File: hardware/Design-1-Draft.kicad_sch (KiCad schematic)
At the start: 32 parts, among them J1 Barrel_Jack_Switch, M1 WATERPUMP-2, M2 WATERPUMP-1, Q1 IRLZ44N, Q2 IRLZ44N, SW1 Button, U1 ADS1115IDGS, U2 Tang_Nano_9K

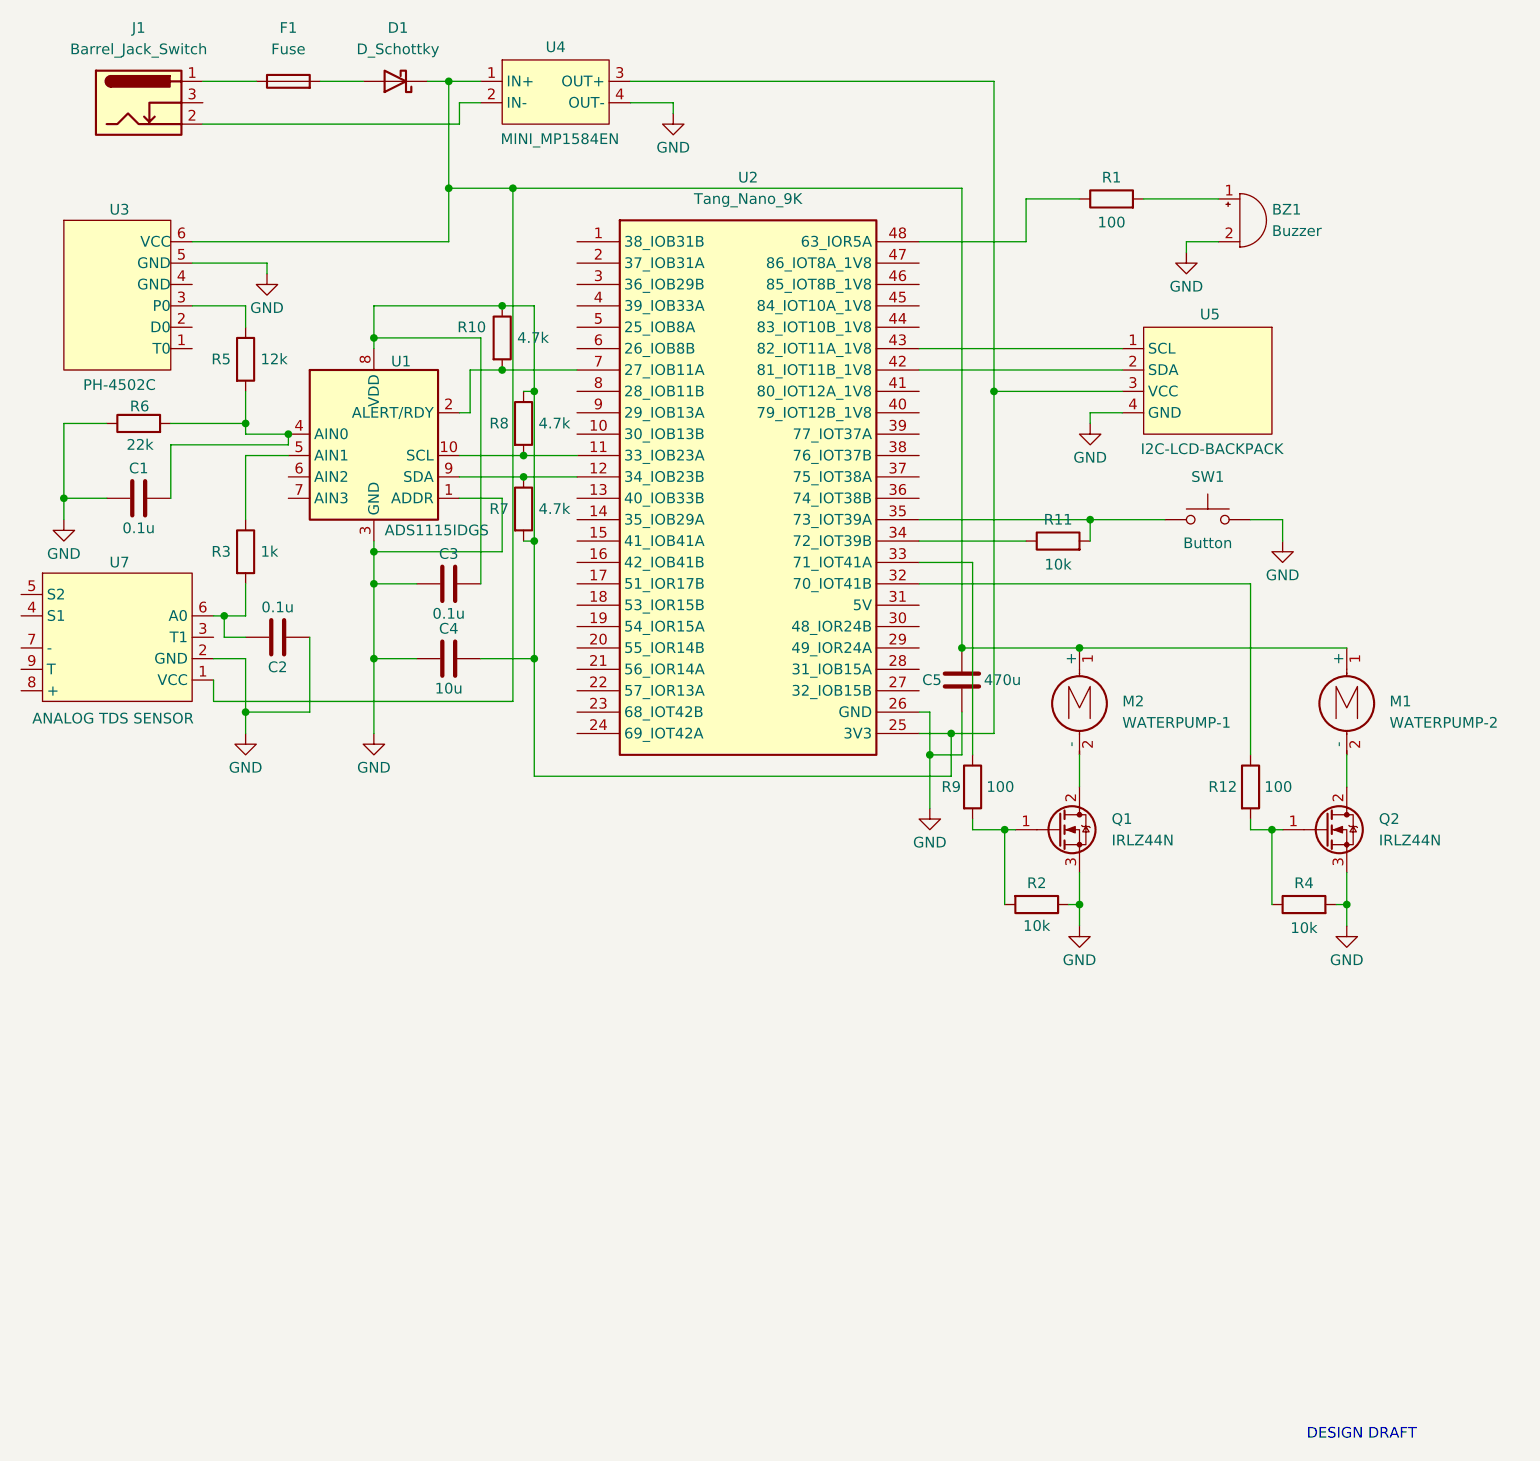
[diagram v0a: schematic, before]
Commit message: Renaming Symbols
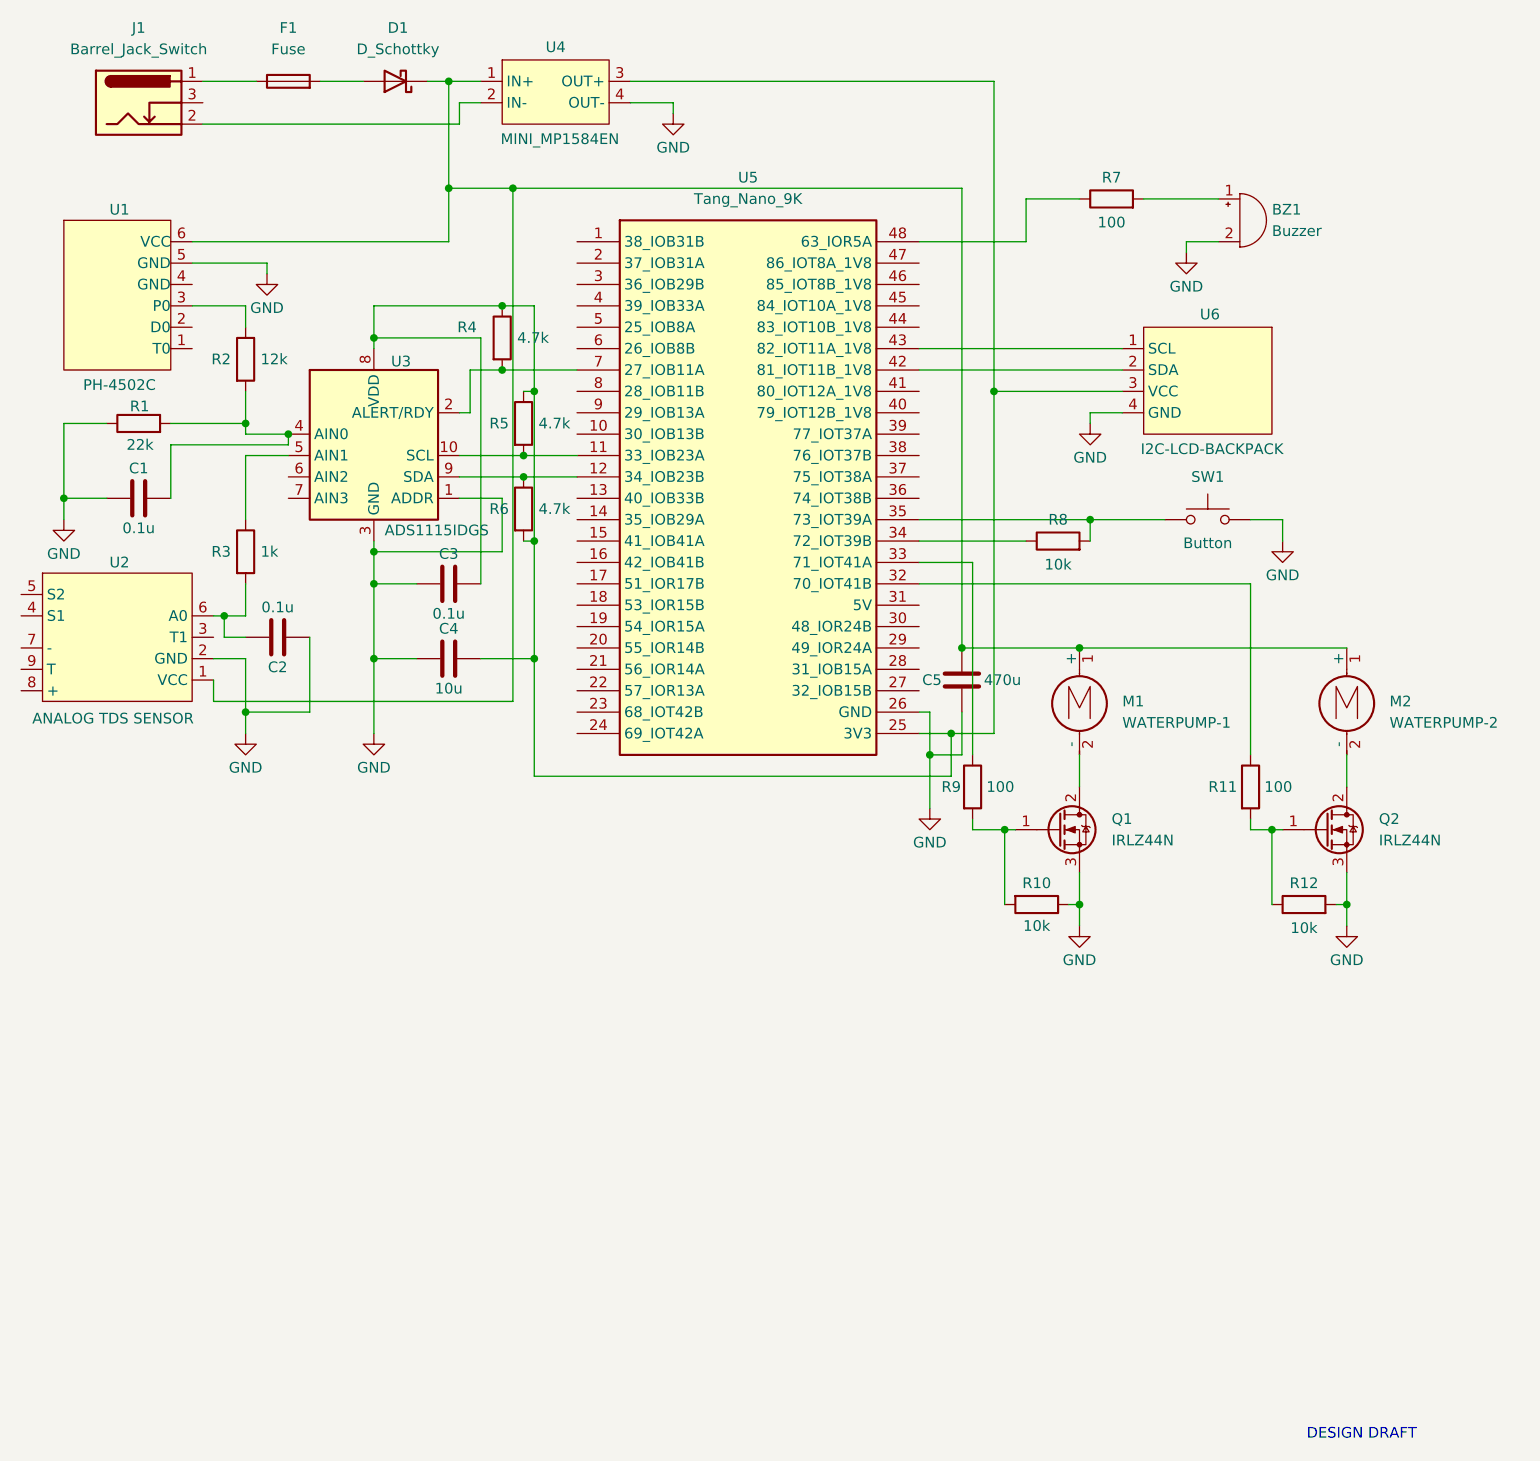
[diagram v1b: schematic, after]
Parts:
- renumbered M2 to M1, M1 to M2, R6 to R1, R2 to R10, R12 to R11, R4 to R12, R5 to R2, R10 to R4, R8 to R5, R7 to R6, R1 to R7, R11 to R8, U3 to U1, U7 to U2, U1 to U3, U2 to U5, U5 to U6
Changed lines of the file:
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@@
 		(on_board yes)
 		(dnp no)
-		(property "Reference" "R2"
+		(property "Reference" "R10"
 			(at 154.94 124.46 90)
 			(effects
@@
 			(project "Design-1-Draft"
 				(path "/9fcc7f51-9e94-44d9-a052-14e93dbf110b"
-					(reference "R2")
+					(reference "R10")
 					(unit 1)
 				)
@@
 		(on_board yes)
 		(dnp no)
-		(property "Reference" "U7"
+		(property "Reference" "U2"
 			(at 45.974 86.36 0)
 			(effects
@@
 			(project ""
 				(path "/9fcc7f51-9e94-44d9-a052-14e93dbf110b"
-					(reference "U7")
+					(reference "U2")
 					(unit 1)
 				)
@@
 		(on_board yes)
 		(dnp no)
-		(property "Reference" "R1"
+		(property "Reference" "R7"
 			(at 163.83 40.64 90)
 			(effects
@@
 			(project "Design-1-Draft"
 				(path "/9fcc7f51-9e94-44d9-a052-14e93dbf110b"
-					(reference "R1")
+					(reference "R7")
 					(unit 1)
 				)
@@
 		(on_board yes)
 		(dnp no)
-		(property "Reference" "R6"
+		(property "Reference" "R1"
 			(at 49.53 67.818 90)
 			(effects
@@
 			(project "Design-1-Draft"
 				(path "/9fcc7f51-9e94-44d9-a052-14e93dbf110b"
-					(reference "R6")
+					(reference "R1")
 					(unit 1)
 				)
@@
 		(on_board yes)
 		(dnp no)
-		(property "Reference" "R8"
+		(property "Reference" "R5"
 			(at 89.916 69.85 0)
 			(effects
@@
 			(project "Design-1-Draft"
 				(path "/9fcc7f51-9e94-44d9-a052-14e93dbf110b"
-					(reference "R8")
+					(reference "R5")
 					(unit 1)
 				)
@@
 		(on_board yes)
 		(dnp no)
-		(property "Reference" "R10"
+		(property "Reference" "R4"
 			(at 86.106 58.42 0)
 			(effects
@@
 			(project "Design-1-Draft"
 				(path "/9fcc7f51-9e94-44d9-a052-14e93dbf110b"
-					(reference "R10")
+					(reference "R4")
 					(unit 1)
 				)
@@
 		(dnp no)
 		(fields_autoplaced yes)
-		(property "Reference" "U2"
+		(property "Reference" "U5"
 			(at 120.65 40.64 0)
 			(effects
@@
 			(project ""
 				(path "/9fcc7f51-9e94-44d9-a052-14e93dbf110b"
-					(reference "U2")
+					(reference "U5")
 					(unit 1)
 				)
@@
 		(dnp no)
 		(fields_autoplaced yes)
-		(property "Reference" "M1"
+		(property "Reference" "M2"
 			(at 196.85 102.8699 0)
 			(effects
@@
 			(project ""
 				(path "/9fcc7f51-9e94-44d9-a052-14e93dbf110b"
-					(reference "M1")
+					(reference "M2")
 					(unit 1)
 				)
@@
 		(on_board yes)
 		(dnp no)
-		(property "Reference" "R7"
+		(property "Reference" "R6"
 			(at 89.916 80.01 0)
 			(effects
@@
 			(project "Design-1-Draft"
 				(path "/9fcc7f51-9e94-44d9-a052-14e93dbf110b"
-					(reference "R7")
+					(reference "R6")
 					(unit 1)
 				)
@@
 		(dnp no)
 		(fields_autoplaced yes)
-		(property "Reference" "M2"
+		(property "Reference" "M1"
 			(at 165.1 102.8699 0)
 			(effects
@@
 			(project ""
 				(path "/9fcc7f51-9e94-44d9-a052-14e93dbf110b"
-					(reference "M2")
+					(reference "M1")
 					(unit 1)
 				)
@@
 		(on_board yes)
 		(dnp no)
-		(property "Reference" "R11"
+		(property "Reference" "R8"
 			(at 157.48 81.28 90)
 			(effects
@@
 			(project "Design-1-Draft"
 				(path "/9fcc7f51-9e94-44d9-a052-14e93dbf110b"
-					(reference "R11")
+					(reference "R8")
 					(unit 1)
 				)
@@
 		(on_board yes)
 		(dnp no)
-		(property "Reference" "U5"
+		(property "Reference" "U6"
 			(at 175.514 56.896 0)
 			(effects
@@
 			(project ""
 				(path "/9fcc7f51-9e94-44d9-a052-14e93dbf110b"
-					(reference "U5")
+					(reference "U6")
 					(unit 1)
 				)
@@
 		(on_board yes)
 		(dnp no)
-		(property "Reference" "U3"
+		(property "Reference" "U1"
 			(at 45.974 44.45 0)
 			(effects
@@
 			(project ""
 				(path "/9fcc7f51-9e94-44d9-a052-14e93dbf110b"
-					(reference "U3")
+					(reference "U1")
 					(unit 1)
 				)
@@
 		(on_board yes)
 		(dnp no)
-		(property "Reference" "U1"
+		(property "Reference" "U3"
 			(at 78.232 62.484 0)
 			(effects
@@
 			(project ""
 				(path "/9fcc7f51-9e94-44d9-a052-14e93dbf110b"
-					(reference "U1")
+					(reference "U3")
 					(unit 1)
 				)
@@
 		(on_board yes)
 		(dnp no)
-		(property "Reference" "R12"
+		(property "Reference" "R11"
 			(at 177.038 113.03 0)
 			(effects
@@
 			(project "Design-1-Draft"
 				(path "/9fcc7f51-9e94-44d9-a052-14e93dbf110b"
-					(reference "R12")
+					(reference "R11")
 					(unit 1)
 				)
@@
 		(on_board yes)
 		(dnp no)
-		(property "Reference" "R5"
+		(property "Reference" "R2"
 			(at 56.896 62.23 0)
 			(effects
@@
 			(project "Design-1-Draft"
 				(path "/9fcc7f51-9e94-44d9-a052-14e93dbf110b"
-					(reference "R5")
+					(reference "R2")
 					(unit 1)
 				)
@@
 		(on_board yes)
 		(dnp no)
-		(property "Reference" "R4"
+		(property "Reference" "R12"
 			(at 186.69 124.46 90)
 			(effects
@@
 			(project "Design-1-Draft"
 				(path "/9fcc7f51-9e94-44d9-a052-14e93dbf110b"
-					(reference "R4")
-					(unit 1)
-				)
+					(reference "R12")
+					(unit 1)
+				)

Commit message: Assigned footprints sa schematic (kulang pa ginagawan ko pa yung iba)
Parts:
- C1, C2, C3, C4: footprint (none) -> Capacitor_SMD:C_0805_2012Metric_Pad1.18x1.45mm_HandSolder
- C5: footprint (none) -> Capacitor_THT:CP_Radial_D6.3mm_P2.50mm
- D1: footprint (none) -> Diode_THT:D_DO-41_SOD81_P10.16mm_Horizontal
- R1, R10, R11, R12, R2, R3, R4, R5, R6, R7, R8, R9: footprint (none) -> Resistor_SMD:R_0805_2012Metric_Pad1.20x1.40mm_HandSolder
- U1: footprint (none) -> 1_CustomFootprints:PH-4502C
- U6: footprint (none) -> 1_CustomFootprints:I2C-BACKPACK-LCD
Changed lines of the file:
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@@
 			)
 		)
-		(property "Footprint" ""
+		(property "Footprint" "Resistor_SMD:R_0805_2012Metric_Pad1.20x1.40mm_HandSolder"
 			(at 154.94 125.222 90)
 			(effects
@@
 			)
 		)
-		(property "Footprint" ""
+		(property "Footprint" "Diode_THT:D_DO-41_SOD81_P10.16mm_Horizontal"
 			(at 78.74 29.21 0)
 			(effects
@@
 			)
 		)
-		(property "Footprint" ""
+		(property "Footprint" "Capacitor_THT:CP_Radial_D6.3mm_P2.50mm"
 			(at 145.0848 96.52 0)
 			(effects
@@
 			)
 		)
-		(property "Footprint" ""
+		(property "Footprint" "Resistor_SMD:R_0805_2012Metric_Pad1.20x1.40mm_HandSolder"
 			(at 163.83 44.958 90)
 			(effects
@@
 			)
 		)
-		(property "Footprint" ""
+		(property "Footprint" "Resistor_SMD:R_0805_2012Metric_Pad1.20x1.40mm_HandSolder"
 			(at 48.26 71.628 90)
 			(effects
@@
 			)
 		)
-		(property "Footprint" ""
+		(property "Footprint" "Resistor_SMD:R_0805_2012Metric_Pad1.20x1.40mm_HandSolder"
 			(at 92.202 69.85 90)
 			(effects
@@
 			)
 		)
-		(property "Footprint" ""
+		(property "Footprint" "Capacitor_SMD:C_0805_2012Metric_Pad1.18x1.45mm_HandSolder"
 			(at 88.9 96.8248 0)
 			(effects
@@
 			)
 		)
-		(property "Footprint" ""
+		(property "Footprint" "Resistor_SMD:R_0805_2012Metric_Pad1.20x1.40mm_HandSolder"
 			(at 59.182 85.09 90)
 			(effects
@@
 			)
 		)
-		(property "Footprint" ""
+		(property "Footprint" "Resistor_SMD:R_0805_2012Metric_Pad1.20x1.40mm_HandSolder"
 			(at 89.662 59.69 90)
 			(effects
@@
 			)
 		)
-		(property "Footprint" ""
+		(property "Footprint" "Resistor_SMD:R_0805_2012Metric_Pad1.20x1.40mm_HandSolder"
 			(at 92.202 80.01 90)
 			(effects
@@
 			)
 		)
-		(property "Footprint" ""
+		(property "Footprint" "Resistor_SMD:R_0805_2012Metric_Pad1.20x1.40mm_HandSolder"
 			(at 157.48 85.598 90)
 			(effects
@@
 			)
 		)
-		(property "Footprint" ""
+		(property "Footprint" "1_CustomFootprints:I2C-BACKPACK-LCD"
 			(at 167.64 71.12 0)
 			(effects
@@
 			)
 		)
-		(property "Footprint" ""
+		(property "Footprint" "Resistor_SMD:R_0805_2012Metric_Pad1.20x1.40mm_HandSolder"
 			(at 145.542 113.03 90)
 			(effects
@@
 			)
 		)
-		(property "Footprint" ""
+		(property "Footprint" "1_CustomFootprints:PH-4502C"
 			(at 52.07 63.5 0)
 			(effects
@@
 			)
 		)
-		(property "Footprint" ""
+		(property "Footprint" "Resistor_SMD:R_0805_2012Metric_Pad1.20x1.40mm_HandSolder"
 			(at 178.562 113.03 90)
 			(effects
@@
 			)
 		)
-		(property "Footprint" ""
+		(property "Footprint" "Resistor_SMD:R_0805_2012Metric_Pad1.20x1.40mm_HandSolder"
 			(at 59.182 62.23 90)
 			(effects
@@
 			)
 		)
-		(property "Footprint" ""
+		(property "Footprint" "Resistor_SMD:R_0805_2012Metric_Pad1.20x1.40mm_HandSolder"
 			(at 186.69 128.778 90)
 			(effects
@@
 			)
 		)
-		(property "Footprint" ""
+		(property "Footprint" "Capacitor_SMD:C_0805_2012Metric_Pad1.18x1.45mm_HandSolder"
 			(at 88.9 87.9348 0)
 			(effects
@@
 			)
 		)
-		(property "Footprint" ""
+		(property "Footprint" "Capacitor_SMD:C_0805_2012Metric_Pad1.18x1.45mm_HandSolder"
 			(at 52.07 77.7748 0)
 			(effects
@@
 			)
 		)
-		(property "Footprint" ""
+		(property "Footprint" "Capacitor_SMD:C_0805_2012Metric_Pad1.18x1.45mm_HandSolder"
 			(at 60.96 96.2152 0)
 			(effects

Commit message: updated footprint lib
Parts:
- C1, C2, C3: footprint Capacitor_SMD:C_0805_2012Metric_Pad1.18x1.45mm_HandSolder -> Capacitor_THT:C_Disc_D5.0mm_W2.5mm_P5.00mm
- C4: footprint Capacitor_SMD:C_0805_2012Metric_Pad1.18x1.45mm_HandSolder -> Capacitor_THT:C_Radial_D6.3mm_H5.0mm_P2.50mm
- C5: footprint Capacitor_THT:CP_Radial_D6.3mm_P2.50mm -> Capacitor_THT:CP_Radial_D10.0mm_P5.00mm
- J1: footprint (none) -> Connector_BarrelJack:BarrelJack_CUI_PJ-102AH_Horizontal
- R1, R10, R11, R12, R2, R3, R4, R5, R6, R7, R8, R9: footprint Resistor_SMD:R_0805_2012Metric_Pad1.20x1.40mm_HandSolder -> Resistor_THT:R_Axial_DIN0207_L6.3mm_D2.5mm_P10.16mm_Horizontal
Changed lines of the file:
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@@
 			)
 		)
-		(property "Footprint" "Resistor_SMD:R_0805_2012Metric_Pad1.20x1.40mm_HandSolder"
+		(property "Footprint" "Resistor_THT:R_Axial_DIN0207_L6.3mm_D2.5mm_P10.16mm_Horizontal"
 			(at 154.94 125.222 90)
 			(effects
@@
 			)
 		)
-		(property "Footprint" "Capacitor_THT:CP_Radial_D6.3mm_P2.50mm"
+		(property "Footprint" "Capacitor_THT:CP_Radial_D10.0mm_P5.00mm"
 			(at 145.0848 96.52 0)
 			(effects
@@
 			)
 		)
-		(property "Footprint" "Resistor_SMD:R_0805_2012Metric_Pad1.20x1.40mm_HandSolder"
+		(property "Footprint" "Resistor_THT:R_Axial_DIN0207_L6.3mm_D2.5mm_P10.16mm_Horizontal"
 			(at 163.83 44.958 90)
 			(effects
@@
 			)
 		)
-		(property "Footprint" "Resistor_SMD:R_0805_2012Metric_Pad1.20x1.40mm_HandSolder"
+		(property "Footprint" "Resistor_THT:R_Axial_DIN0207_L6.3mm_D2.5mm_P10.16mm_Horizontal"
 			(at 48.26 71.628 90)
 			(effects
@@
 			)
 		)
-		(property "Footprint" "Resistor_SMD:R_0805_2012Metric_Pad1.20x1.40mm_HandSolder"
+		(property "Footprint" "Resistor_THT:R_Axial_DIN0207_L6.3mm_D2.5mm_P10.16mm_Horizontal"
 			(at 92.202 69.85 90)
 			(effects
@@
 			)
 		)
-		(property "Footprint" "Capacitor_SMD:C_0805_2012Metric_Pad1.18x1.45mm_HandSolder"
+		(property "Footprint" "Capacitor_THT:C_Radial_D6.3mm_H5.0mm_P2.50mm"
 			(at 88.9 96.8248 0)
 			(effects
@@
 			)
 		)
-		(property "Footprint" "Resistor_SMD:R_0805_2012Metric_Pad1.20x1.40mm_HandSolder"
+		(property "Footprint" "Resistor_THT:R_Axial_DIN0207_L6.3mm_D2.5mm_P10.16mm_Horizontal"
 			(at 59.182 85.09 90)
 			(effects
@@
 			)
 		)
-		(property "Footprint" "Resistor_SMD:R_0805_2012Metric_Pad1.20x1.40mm_HandSolder"
+		(property "Footprint" "Resistor_THT:R_Axial_DIN0207_L6.3mm_D2.5mm_P10.16mm_Horizontal"
 			(at 89.662 59.69 90)
 			(effects
@@
 			)
 		)
-		(property "Footprint" "Resistor_SMD:R_0805_2012Metric_Pad1.20x1.40mm_HandSolder"
+		(property "Footprint" "Resistor_THT:R_Axial_DIN0207_L6.3mm_D2.5mm_P10.16mm_Horizontal"
 			(at 92.202 80.01 90)
 			(effects
@@
 			)
 		)
-		(property "Footprint" "Resistor_SMD:R_0805_2012Metric_Pad1.20x1.40mm_HandSolder"
+		(property "Footprint" "Resistor_THT:R_Axial_DIN0207_L6.3mm_D2.5mm_P10.16mm_Horizontal"
 			(at 157.48 85.598 90)
 			(effects
@@
 			)
 		)
-		(property "Footprint" "Resistor_SMD:R_0805_2012Metric_Pad1.20x1.40mm_HandSolder"
+		(property "Footprint" "Resistor_THT:R_Axial_DIN0207_L6.3mm_D2.5mm_P10.16mm_Horizontal"
 			(at 145.542 113.03 90)
 			(effects
@@
 			)
 		)
-		(property "Footprint" "Resistor_SMD:R_0805_2012Metric_Pad1.20x1.40mm_HandSolder"
+		(property "Footprint" "Resistor_THT:R_Axial_DIN0207_L6.3mm_D2.5mm_P10.16mm_Horizontal"
 			(at 178.562 113.03 90)
 			(effects
@@
 			)
 		)
-		(property "Footprint" "Resistor_SMD:R_0805_2012Metric_Pad1.20x1.40mm_HandSolder"
+		(property "Footprint" "Resistor_THT:R_Axial_DIN0207_L6.3mm_D2.5mm_P10.16mm_Horizontal"
 			(at 59.182 62.23 90)
 			(effects
@@
 			)
 		)
-		(property "Footprint" "Resistor_SMD:R_0805_2012Metric_Pad1.20x1.40mm_HandSolder"
+		(property "Footprint" "Resistor_THT:R_Axial_DIN0207_L6.3mm_D2.5mm_P10.16mm_Horizontal"
 			(at 186.69 128.778 90)
 			(effects
@@
 			)
 		)
-		(property "Footprint" "Capacitor_SMD:C_0805_2012Metric_Pad1.18x1.45mm_HandSolder"
+		(property "Footprint" "Capacitor_THT:C_Disc_D5.0mm_W2.5mm_P5.00mm"
 			(at 88.9 87.9348 0)
 			(effects
@@
 			)
 		)
-		(property "Footprint" ""
+		(property "Footprint" "Connector_BarrelJack:BarrelJack_CUI_PJ-102AH_Horizontal"
 			(at 49.53 32.766 0)
 			(effects
@@
 			)
 		)
-		(property "Footprint" "Capacitor_SMD:C_0805_2012Metric_Pad1.18x1.45mm_HandSolder"
+		(property "Footprint" "Capacitor_THT:C_Disc_D5.0mm_W2.5mm_P5.00mm"
 			(at 52.07 77.7748 0)
 			(effects
@@
 			)
 		)
-		(property "Footprint" "Capacitor_SMD:C_0805_2012Metric_Pad1.18x1.45mm_HandSolder"
+		(property "Footprint" "Capacitor_THT:C_Disc_D5.0mm_W2.5mm_P5.00mm"
 			(at 60.96 96.2152 0)
 			(effects

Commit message: updated footprints
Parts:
- M1, M2: footprint (none) -> Connector_PinHeader_2.54mm:PinHeader_1x02_P2.54mm_Vertical
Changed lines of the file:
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@@
 			)
 		)
-		(property "Footprint" ""
+		(property "Footprint" "Connector_PinHeader_2.54mm:PinHeader_1x02_P2.54mm_Vertical"
 			(at 191.77 103.886 0)
 			(effects
@@
 			)
 		)
-		(property "Footprint" ""
+		(property "Footprint" "Connector_PinHeader_2.54mm:PinHeader_1x02_P2.54mm_Vertical"
 			(at 160.02 103.886 0)
 			(effects
